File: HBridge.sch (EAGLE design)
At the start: 40 parts, among them IC1 74HC08D, IC2 A4954, SW1 SWITCH-DP3T, SW2 SWITCH-DP3T

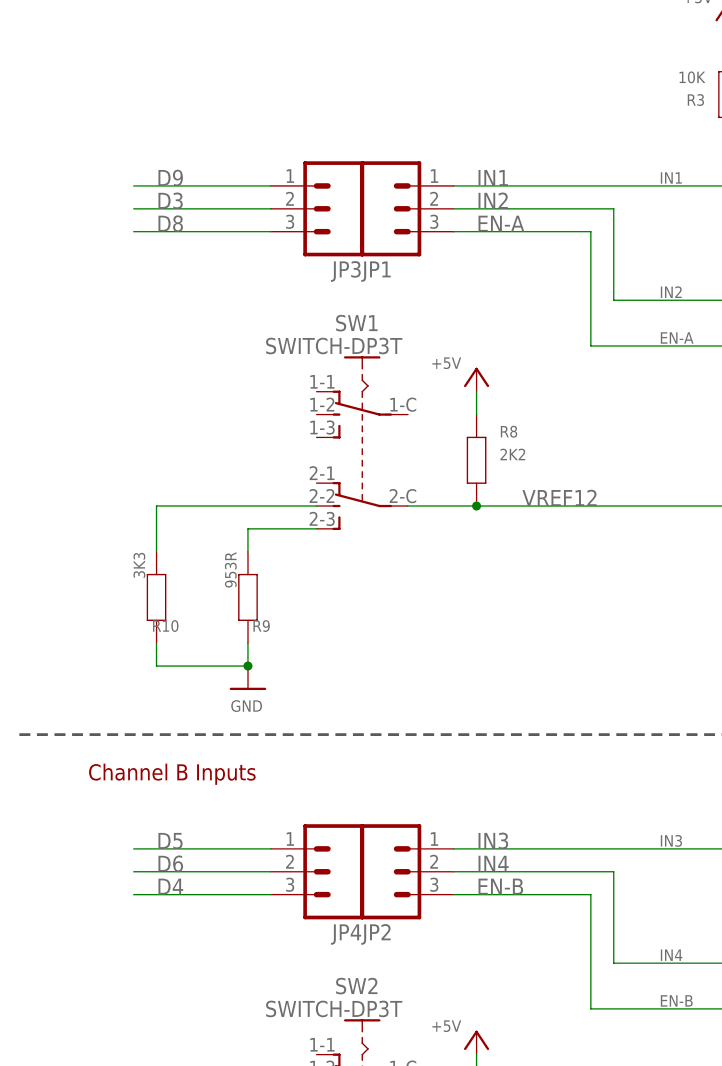
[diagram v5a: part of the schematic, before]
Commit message: Changed input pins; rerouted; ERC and DRC
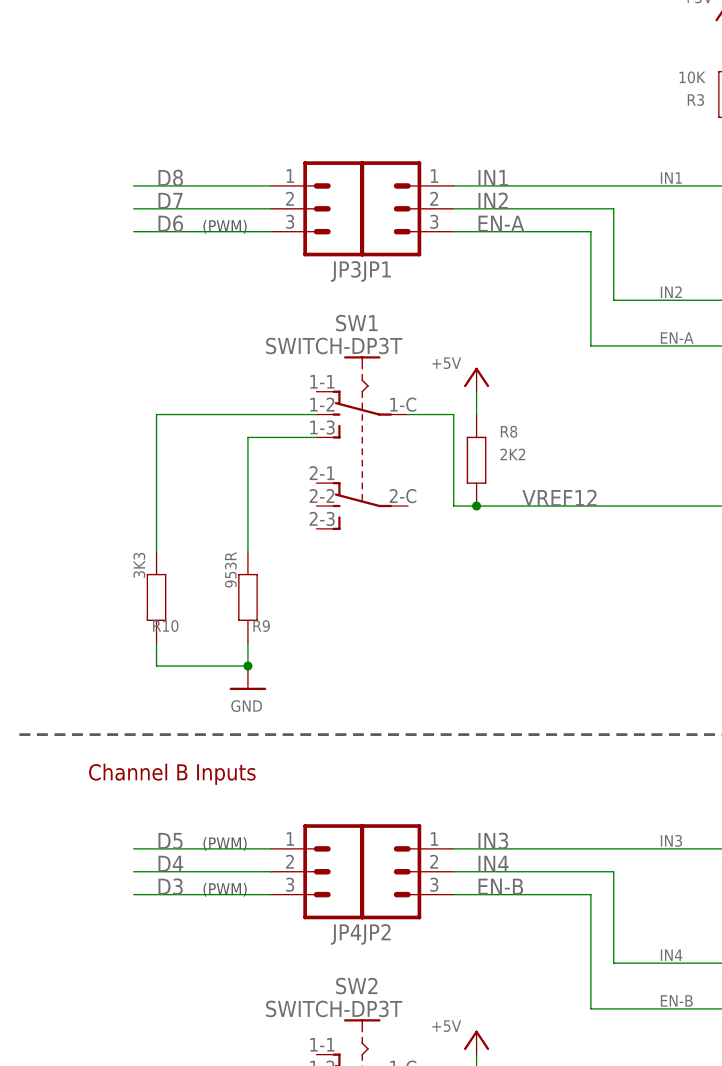
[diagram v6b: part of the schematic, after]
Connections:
- net D3: now also JP4.3; no longer JP3.2
- net D4: now also JP4.2; no longer JP4.3
- net D6: now also JP3.3; no longer JP4.2
- net D7: now also JP3.2
- net D8: now also JP3.1; no longer JP3.3
- net D9: no longer JP3.1
- net N$15: now also SW1.1-2; no longer SW1.2-2
- net N$21: now also SW1.1-3; no longer SW1.2-3
- net VREF12: now also SW1.1-C; no longer SW1.2-C
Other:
- note added: "(PWM)"
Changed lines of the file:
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@@
 <text x="12.7" y="363.22" size="1.778" layer="94" ratio="15">Channel A Inputs</text>
 <text x="12.7" y="274.32" size="1.778" layer="94" ratio="15">Channel B Inputs</text>
+<text x="25.4" y="335.28" size="1.27" layer="97" ratio="15">(PWM)</text>
+<text x="25.4" y="261.62" size="1.27" layer="97" ratio="15">(PWM)</text>
+<text x="25.4" y="266.7" size="1.27" layer="97" ratio="15">(PWM)</text>
 </plain>
 <instances>
@@
 <pinref part="H1" gate="G$1" pin="2"/>
 </segment>
-<segment>
-<pinref part="JP3" gate="G$1" pin="1"/>
-<wire x1="33.02" y1="340.36" x2="17.78" y2="340.36" width="0.1524" layer="91"/>
-<label x="20.32" y="340.36" size="1.778" layer="95"/>
-</segment>
 </net>
 <net name="D8" class="0">
@@
 </segment>
 <segment>
-<pinref part="JP3" gate="G$1" pin="3"/>
-<wire x1="33.02" y1="335.28" x2="17.78" y2="335.28" width="0.1524" layer="91"/>
-<label x="20.32" y="335.28" size="1.778" layer="95"/>
+<pinref part="JP3" gate="G$1" pin="1"/>
+<wire x1="33.02" y1="340.36" x2="17.78" y2="340.36" width="0.1524" layer="91"/>
+<label x="20.32" y="340.36" size="1.778" layer="95"/>
 </segment>
 </net>
@@
 <pinref part="H2" gate="G$1" pin="8"/>
 </segment>
+<segment>
+<pinref part="JP3" gate="G$1" pin="2"/>
+<wire x1="33.02" y1="337.82" x2="17.78" y2="337.82" width="0.1524" layer="91"/>
+<label x="20.32" y="337.82" size="1.778" layer="95"/>
+</segment>
 </net>
 <net name="D6" class="0">
@@
 </segment>
 <segment>
-<pinref part="JP4" gate="G$1" pin="2"/>
-<wire x1="33.02" y1="264.16" x2="17.78" y2="264.16" width="0.1524" layer="91"/>
-<label x="20.32" y="264.16" size="1.778" layer="95"/>
+<pinref part="JP3" gate="G$1" pin="3"/>
+<wire x1="33.02" y1="335.28" x2="17.78" y2="335.28" width="0.1524" layer="91"/>
+<label x="20.32" y="335.28" size="1.778" layer="95"/>
 </segment>
 </net>
@@
 </segment>
 <segment>
-<pinref part="JP4" gate="G$1" pin="3"/>
-<wire x1="33.02" y1="261.62" x2="17.78" y2="261.62" width="0.1524" layer="91"/>
-<label x="20.32" y="261.62" size="1.778" layer="95"/>
+<pinref part="JP4" gate="G$1" pin="2"/>
+<wire x1="33.02" y1="264.16" x2="17.78" y2="264.16" width="0.1524" layer="91"/>
+<label x="20.32" y="264.16" size="1.778" layer="95"/>
 </segment>
 </net>
@@
 </segment>
 <segment>
-<pinref part="JP3" gate="G$1" pin="2"/>
-<wire x1="33.02" y1="337.82" x2="17.78" y2="337.82" width="0.1524" layer="91"/>
-<label x="20.32" y="337.82" size="1.778" layer="95"/>
+<pinref part="JP4" gate="G$1" pin="3"/>
+<wire x1="33.02" y1="261.62" x2="17.78" y2="261.62" width="0.1524" layer="91"/>
+<label x="20.32" y="261.62" size="1.778" layer="95"/>
 </segment>
 </net>
@@
 <segment>
 <pinref part="R8" gate="G$1" pin="2"/>
-<pinref part="SW1" gate="G$1" pin="2-C"/>
-<wire x1="48.26" y1="304.8" x2="55.88" y2="304.8" width="0.1524" layer="91"/>
-<junction x="55.88" y="304.8"/>
 <label x="60.96" y="304.8" size="1.778" layer="95"/>
 <pinref part="IC2" gate="G$1" pin="VREF12"/>
 <wire x1="55.88" y1="304.8" x2="144.78" y2="304.8" width="0.1524" layer="91"/>
 <label x="111.76" y="304.8" size="1.778" layer="95"/>
+<wire x1="55.88" y1="304.8" x2="53.34" y2="304.8" width="0.1524" layer="91"/>
+<wire x1="53.34" y1="304.8" x2="53.34" y2="314.96" width="0.1524" layer="91"/>
+<pinref part="SW1" gate="G$1" pin="1-C"/>
+<wire x1="53.34" y1="314.96" x2="48.26" y2="314.96" width="0.1524" layer="91"/>
+<junction x="55.88" y="304.8"/>
 </segment>
 </net>
@@
 <segment>
 <pinref part="R10" gate="G$1" pin="1"/>
-<wire x1="20.32" y1="299.72" x2="20.32" y2="304.8" width="0.1524" layer="91"/>
-<pinref part="SW1" gate="G$1" pin="2-2"/>
-<wire x1="20.32" y1="304.8" x2="38.1" y2="304.8" width="0.1524" layer="91"/>
+<wire x1="20.32" y1="299.72" x2="20.32" y2="314.96" width="0.1524" layer="91"/>
+<pinref part="SW1" gate="G$1" pin="1-2"/>
+<wire x1="20.32" y1="314.96" x2="38.1" y2="314.96" width="0.1524" layer="91"/>
 </segment>
 </net>
@@
 <segment>
 <pinref part="R9" gate="G$1" pin="1"/>
-<wire x1="30.48" y1="299.72" x2="30.48" y2="302.26" width="0.1524" layer="91"/>
-<pinref part="SW1" gate="G$1" pin="2-3"/>
-<wire x1="30.48" y1="302.26" x2="38.1" y2="302.26" width="0.1524" layer="91"/>
-</segment>
-</net>
+<wire x1="30.48" y1="299.72" x2="30.48" y2="312.42" width="0.1524" layer="91"/>
+<pinref part="SW1" gate="G$1" pin="1-3"/>
+<wire x1="30.48" y1="312.42" x2="38.1" y2="312.42" width="0.1524" layer="91"/>
+</segment>
+</net>

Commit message: Annotation updates for release
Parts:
- removed J3: (no value), freetronics-master-v1:M02PTH
- removed JP4: (no value), freetronics-master-v1.1:M03PTH
- removed R12: 2K2, freetronics-master-v1:RESISTOR0603
- removed SW1: SWITCH-DP3T, freetronics-jon:SWITCH-DP3T
- added R2: 10K 0603, freetronics-master-v1:RESISTOR0603
- added S3: RESET, freetronics-master-v1:TAC_SWITCH_2PIN
- C1, C4: value 100nF -> 100nF 0603
- C2: value 100uF -> 100uF 50V
- C3: value 220nF -> 220nF 50V 0603
- IC1: value 74HC08D -> 74HC08D SOIC-14
- IC2: value A4954 -> A4954 TSSOP-16
- JP1, JP2: device freetronics-master-v1.1:M03PTH -> freetronics-master-v1:PINHD-2X3
- JP3: device freetronics-master-v1.1:M03PTH -> freetronics-master-v1:M02PTH
- R1: value 3K3 -> 10K 0603
- R10: value 3K3 -> 0.25R 1W 2010; device freetronics-master-v1:RESISTOR0603 -> rcl:R-EU_R2010
- R11: value 953R -> 2K2 0603; device freetronics-master-v1:RESISTOR0603 -> freetronics:RESISTOR0603
- R3: value 10K -> 2K2 0603
- R4: value 10K -> 3K3 1% 0603
- R5: value 0.25R 1W -> 953R 1% 0603; device rcl:R-EU_R2010 -> freetronics-master-v1:RESISTOR0603
- R6: value 0.25R 1W -> 2K2 0603; device rcl:R-EU_R2010 -> freetronics-master-v1:RESISTOR0603
- R7: value 2K2 -> 3K3 1% 0603; device freetronics:RESISTOR0603 -> freetronics-master-v1:RESISTOR0603
- R8: value 2K2 -> 953R 1% 0603
- R9: value 953R -> 0.25R 1W 2010; device freetronics-master-v1:RESISTOR0603 -> rcl:R-EU_R2010
- S1: value RESET -> SWITCH-DP3T MS-23C01; device freetronics-master-v1:TAC_SWITCH_2PIN -> freetronics-jon:SWITCH-DP3T
- S2: value SWITCH-DP3T -> SWITCH-DP3T MS-23C01
- renumbered C5 to C2, C6 to C1, C7 to C3, C8 to C4, SW2 to S2
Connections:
- net +5V: now also R1.1, R11.1, R2.2, R6.1; no longer R12.1, R4.2, R7.1, R8.1
- net D2: now also JP2.4
- net D3: now also JP2.2; no longer JP4.3
- net D4: now also JP1.2; no longer JP4.2
- net D5: now also JP2.6; no longer JP4.1
- net D6: now also JP1.6; no longer JP3.3
- net D7: now also JP1.4; no longer JP3.2
- net D8: no longer JP3.1
- net EN-A: now also JP1.5, R1.2; no longer JP1.3, R3.2
- net EN-B: now also JP2.5, R2.1; no longer JP2.3, R4.1
- net GND: now also R10.1, R4.2, R5.2, R7.2, R8.2, R9.1, S3.S; no longer R1.2, R10.2, R11.2, R5.1, R6.1, R9.2, S1.S
- net IN2: now also JP1.3; no longer JP1.2
- net IN4: now also JP2.3; no longer JP2.2
- net N$13: now also R9.2; no longer R5.2
- net N$14: now also R10.2; no longer R6.2
- net N$15: now also R4.1, S1.1-2; no longer R10.1, SW1.1-2
- net N$21: now also R5.1, S1.1-3; no longer R9.1, SW1.1-3
- net N$22: now also R11.2; no longer R7.2
- net N$4: now also R8.1; no longer R11.1
- net N$49: now also R7.1; no longer R1.1
- net RESET: now also S3.P; no longer S1.P
- net VBB: now also JP3.2; no longer J3.2
- net VIN: now also JP3.1; no longer J3.1
- net VREF12: now also R3.2, S1.1-C; no longer R8.2, SW1.1-C
- net VREF34: now also R6.2; no longer R12.2
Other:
- note added: "(OC0A)"
- note added: "(OC0B)"
- note added: "(OC2B)"
- note added: "Ch A Enable: D6 (OC0A) Ch A Input 1: D4 Ch A Input 2: D7 Ch B Enable: D5 (OC0B) Ch B Input 3: D3 Ch B Input 4: D2"
- note added: "Freetronics H-Bridge Motor Shield"
- note added: "Released under the terms of the TAPR Open Hardware License www.tapr.org/OHL"
- note added: "V1.1 (2013-05-14)"
- note added: "www.freetronics.com/hbridge"
- note removed: "0603"
- note removed: "14-SOIC"
- note removed: "16-TSSOP"
- note removed: "2010"
- note removed: "Freetronics H-Bridge Shield"
- note removed: "V1.0 (2012-25-07)"
- note removed: "www.freetronics.com"
- moved on the sheet: R1, R10, R11, R3, R4, R5, R6, R7, R8, R9

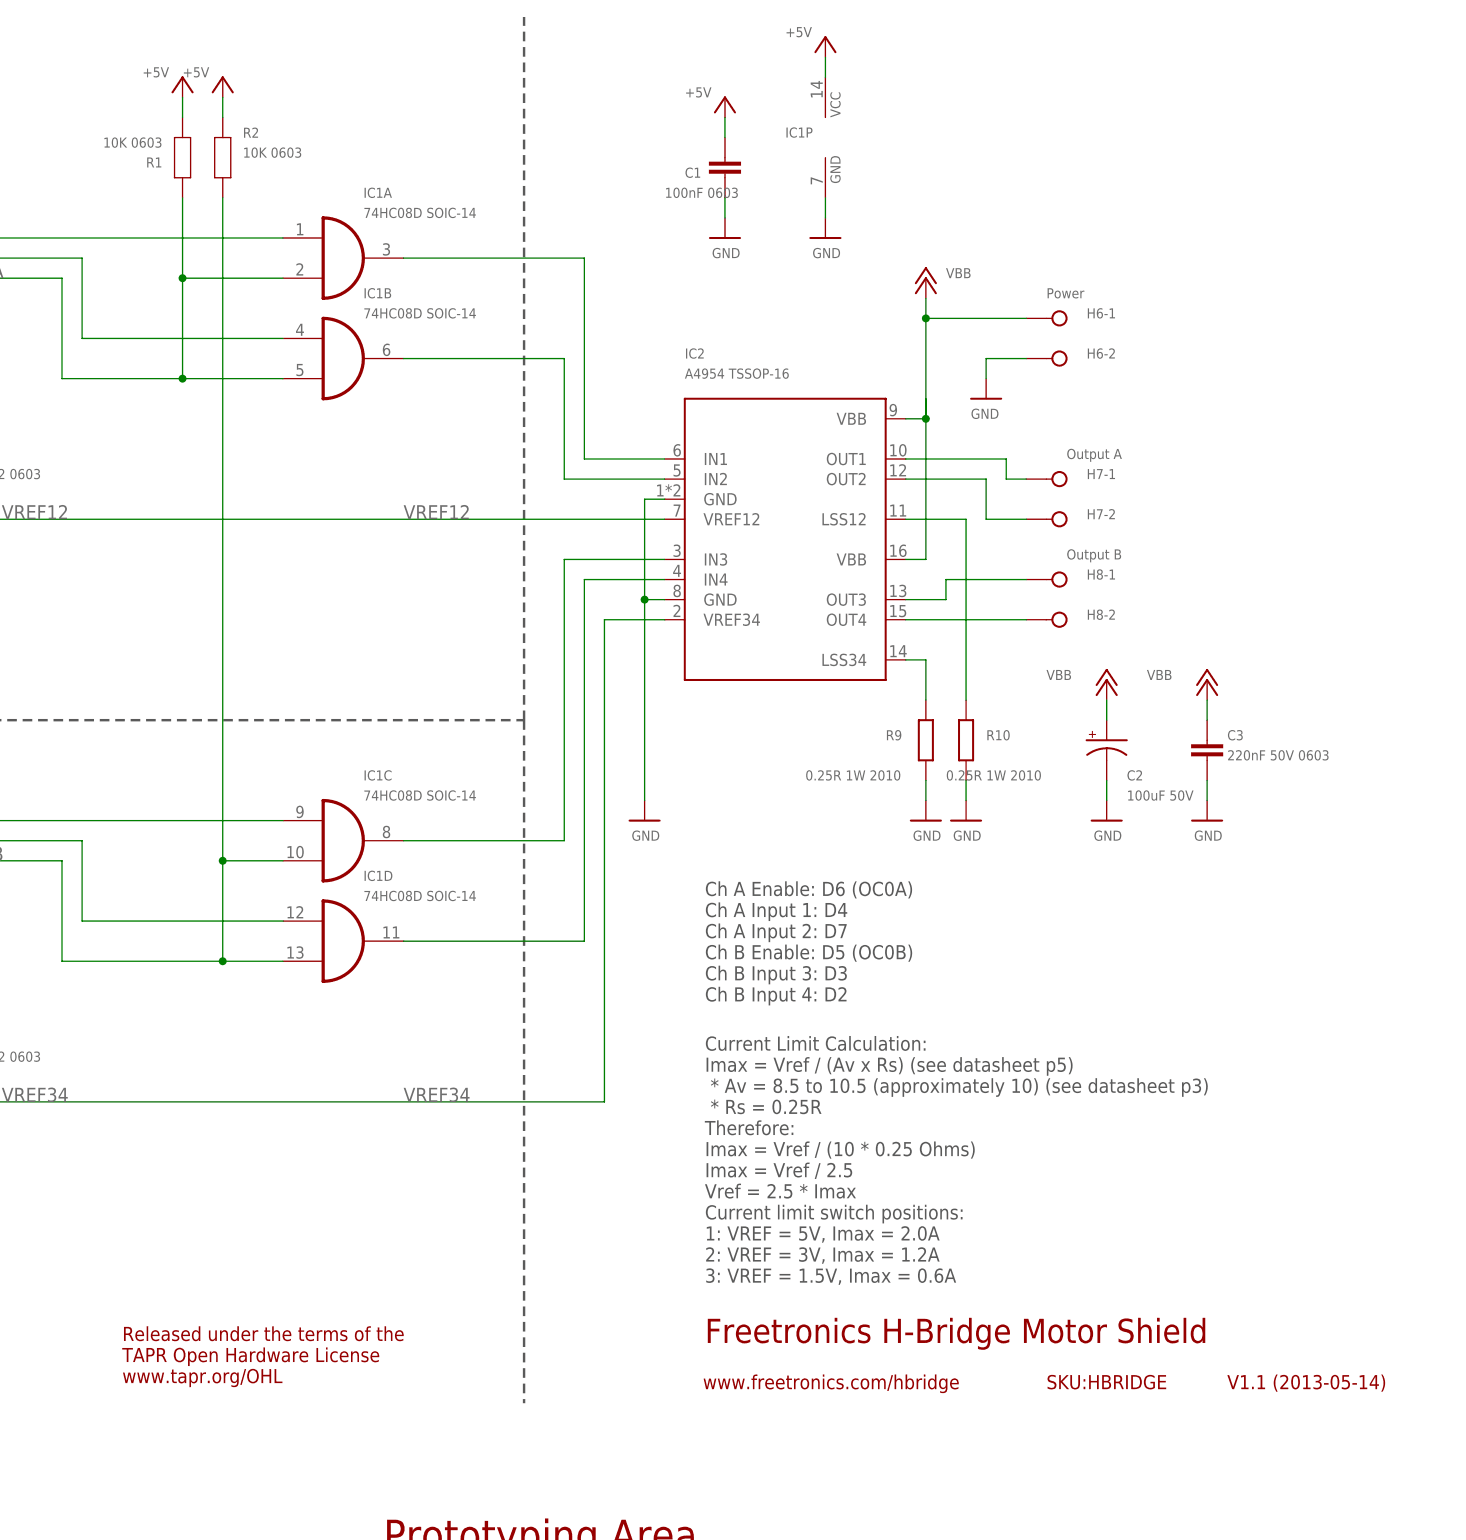
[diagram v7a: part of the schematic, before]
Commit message: Version 1.2: 3.3V compatibility via the IORef pin on Arduino R3
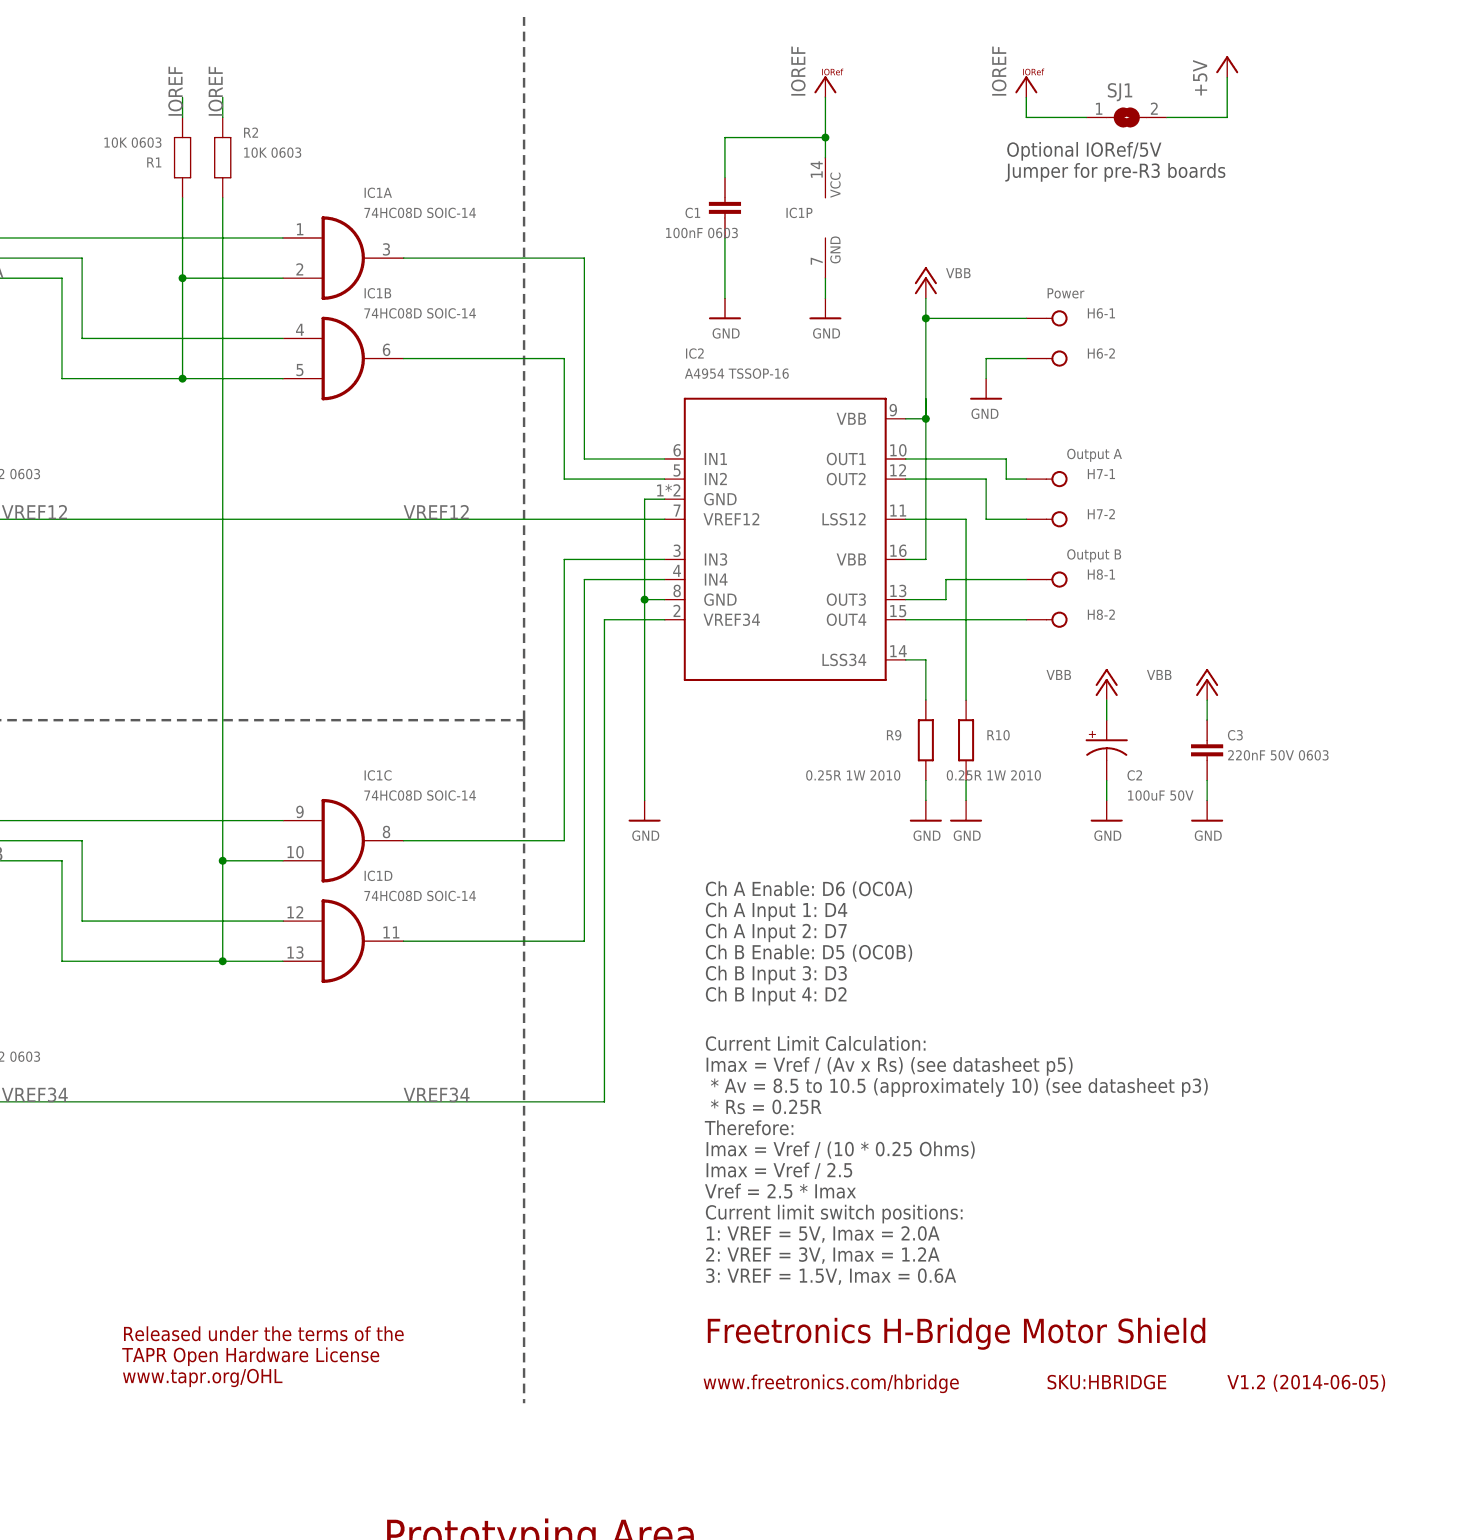
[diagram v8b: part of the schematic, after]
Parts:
- added SJ1: (no value), freetronics-master-v1.1:SJ
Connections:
- net +5V: now also SJ1.2; no longer C1.1, IC1P.VCC, R1.1, R2.2
- net IOREF: now also C1.1, IC1P.VCC, R1.1, R2.2, SJ1.1
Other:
- note added: "Optional IORef/5V Jumper for pre-R3 boards"
- note added: "V1.2 (2014-06-05)"
- note removed: "V1.1 (2013-05-14)"
- moved on the sheet: C1, IC1P
